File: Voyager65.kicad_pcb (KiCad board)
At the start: 2 copper layers, 303.2 x 94.5 mm, 215 parts, among them P1 TC2030-IDC, SW1 SW_PUSH, U1 ATXMEGA32A4U-AU, U2 MCP1700T-3002E/TT, U3 PRTR5V0U2X, U4 IS31FL3733, U5 74LVC1G34

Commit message: Start adding mounts
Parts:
- added REF**: MountingHole_2.2mm_M2_Pad_Via, Mounting_Holes:MountingHole_2.2mm_M2_Pad_Via, F.Cu at (333.4, 66.7)
- added REF**: MountingHole_2.2mm_M2_Pad_Via, Mounting_Holes:MountingHole_2.2mm_M2_Pad_Via, F.Cu at (314.3, 125.4)
- added REF**: MountingHole_2.2mm_M2_Pad_Via, Mounting_Holes:MountingHole_2.2mm_M2_Pad_Via, F.Cu at (100.0, 125.4)
- added REF**: MountingHole_2.2mm_M2_Pad_Via, Mounting_Holes:MountingHole_2.2mm_M2_Pad_Via, F.Cu at (176.2, 95.2)
- added REF**: MountingHole_2.2mm_M2_Pad_Via, Mounting_Holes:MountingHole_2.2mm_M2_Pad_Via, F.Cu at (201.6, 133.3)
- added REF**: MountingHole_2.2mm_M2_Pad_Via, Mounting_Holes:MountingHole_2.2mm_M2_Pad_Via, F.Cu at (66.7, 66.7)
- moved D67 34.1 mm to (163.5, 133.3)
- moved D35 15.1 mm to (158.8, 95.2)
- moved R6 4.99 mm to (60.2, 57.1)
- moved U3 3.87 mm to (66.4, 58.5)
- moved R7 1.81 mm to (70.0, 59.6)
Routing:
- net Net-(D35-Pad2): track 6.02 -> 15.5 mm
- net +5V: track 711.4 -> 717.6 mm
- net Net-(R6-Pad2): track 4.28 -> 7.37 mm, vias 0 -> 2
- net Net-(LED10-Pad2): track 60.6 -> 62.8 mm
- net COL2: track 112.1 -> 113.9 mm
- net LED-SW5: track 377.2 -> 378.9 mm
- net D-: track 50.6 -> 52.1 mm
- net D+: track 48.0 -> 49.6 mm
- net Net-(LED2-Pad2): track 62.8 -> 64.1 mm
- net VCC: track 23.1 -> 21.9 mm
- net Net-(D67-Pad2): track 32.9 -> 34.0 mm
- net LED-CS3: track 116.7 -> 117.6 mm
- net ROW4: track 314.0 -> 314.8 mm
- net GND: track 2107.0 -> 2107.7 mm
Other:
- net class Default: clearance 0.254 -> 0.1524
- net class Power: clearance 0.254 -> 0.1524
- rule trace_clearance: 0.254 -> 0.1524

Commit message: Add mounts
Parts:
- added REF**: MountingHole_2.2mm_M2_Pad_Via, Mounting_Holes:MountingHole_2.2mm_M2_Pad_Via, F.Cu at (128.6, 133.3)
- added REF**: MountingHole_2.2mm_M2_Pad_Via, Mounting_Holes:MountingHole_2.2mm_M2_Pad_Via, F.Cu at (257.2, 123.8)
- added REF**: MountingHole_2.2mm_M2_Pad_Via, Mounting_Holes:MountingHole_2.2mm_M2_Pad_Via, F.Cu at (253.2, 66.7)
- added REF**: MountingHole_2.2mm_M2_Pad_Via, Mounting_Holes:MountingHole_2.2mm_M2_Pad_Via, F.Cu at (158.0, 66.7)
- moved REF** 28.1 mm to (73.0, 133.3)
- moved D63 17.5 mm to (51.6, 133.3)
- moved REF** 14.4 mm to (51.6, 123.3)
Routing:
- net GND: track 2107.7 -> 2162.5 mm, vias 82 -> 85
- net ROW4: track 314.8 -> 332.4 mm
- net Net-(D63-Pad2): track 10.6 -> 16.7 mm, vias 0 -> 1
- net +5V: track 717.6 -> 722.7 mm
- net LED-CS2: track 123.6 -> 126.9 mm
- net Net-(LED4-Pad2): track 70.7 -> 73.4 mm
- net Net-(LED7-Pad2): track 47.4 -> 49.7 mm
- net Net-(LED3-Pad2): track 47.4 -> 49.7 mm
- net Net-(LED10-Pad2): track 62.8 -> 60.6 mm
- net COL2: track 113.9 -> 112.1 mm
- net LED-SW1: track 358.3 -> 359.2 mm
- net LED-CS3: track 117.6 -> 116.7 mm
- net ROW2: track 300.7 -> 301.4 mm
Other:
- board text added: "PCB by ai03, Revision 3.0 60% PCB footprint by amtra5 Design guidance by _spindle and Wilba"
- board text added: "Rev 3.0"
- board text removed: "PCB by ai03, Revision 2.1 60% PCB footprint by amtra5 Design guidance by _spindle and Wilba"
- board text removed: "Rev 2.1"

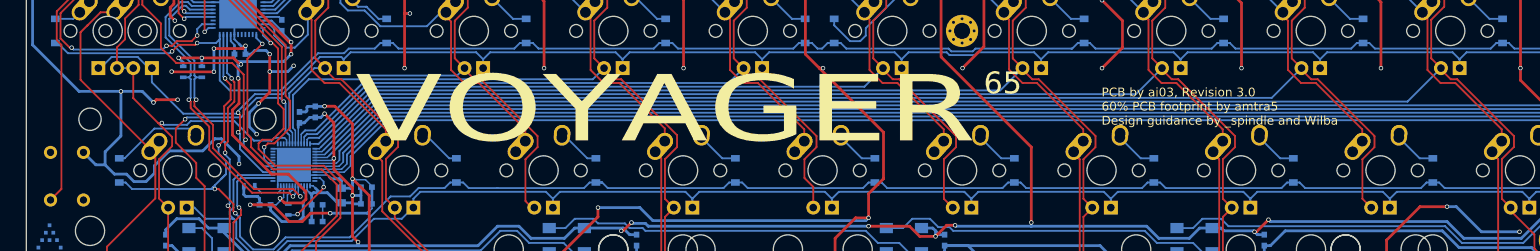
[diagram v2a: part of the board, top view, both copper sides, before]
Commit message: Replace reset switch
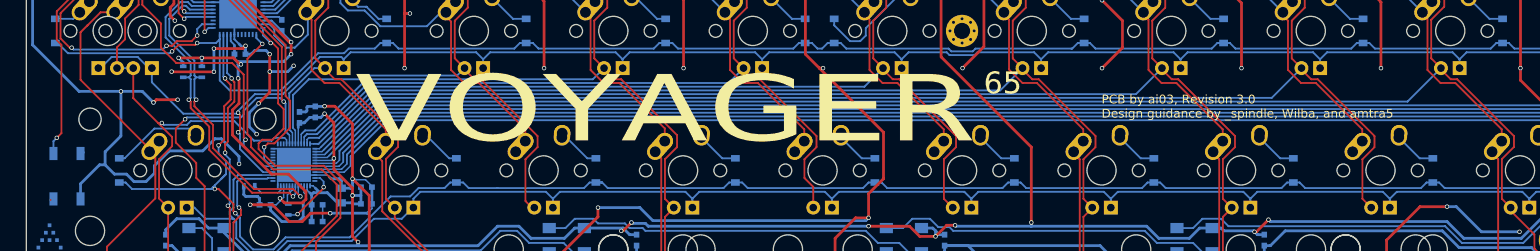
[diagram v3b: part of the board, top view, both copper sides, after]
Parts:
- SW1: footprint Molex-0548190589:PushButton_6x6mm_TH -> Molex-0548190589:SKQG-1155865
- turned SW1 to 270 degrees
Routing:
- net PDI_CLK: track 65.1 -> 58.6 mm, vias 0 -> 1
- net GND: track 2162.5 -> 2165.3 mm
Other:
- board text added: "PCB by ai03, Revision 3.0 Design guidance by _spindle, Wilba, and amtra5"
- board text removed: "PCB by ai03, Revision 3.0 60% PCB footprint by amtra5 Design guidance by _spindle and Wilba"

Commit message: Nudge some traces
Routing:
- net ROW1: track 317.1 -> 318.7 mm
- net LED-SW4: track 359.5 -> 358.1 mm
- net LED-SW3: track 332.3 -> 330.9 mm
- net LED-SW2: track 317.4 -> 316.2 mm
- net ROW2: track 301.4 -> 302.5 mm
- net ROW3: track 316.5 -> 317.7 mm
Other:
- board text added: "PCB by ai03, Revision 3.0 Design guidance by _spindle, Wilba, amtra5, et al."
- board text removed: "PCB by ai03, Revision 3.0 Design guidance by _spindle, Wilba, and amtra5"
